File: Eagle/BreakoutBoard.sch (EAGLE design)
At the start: 13 parts

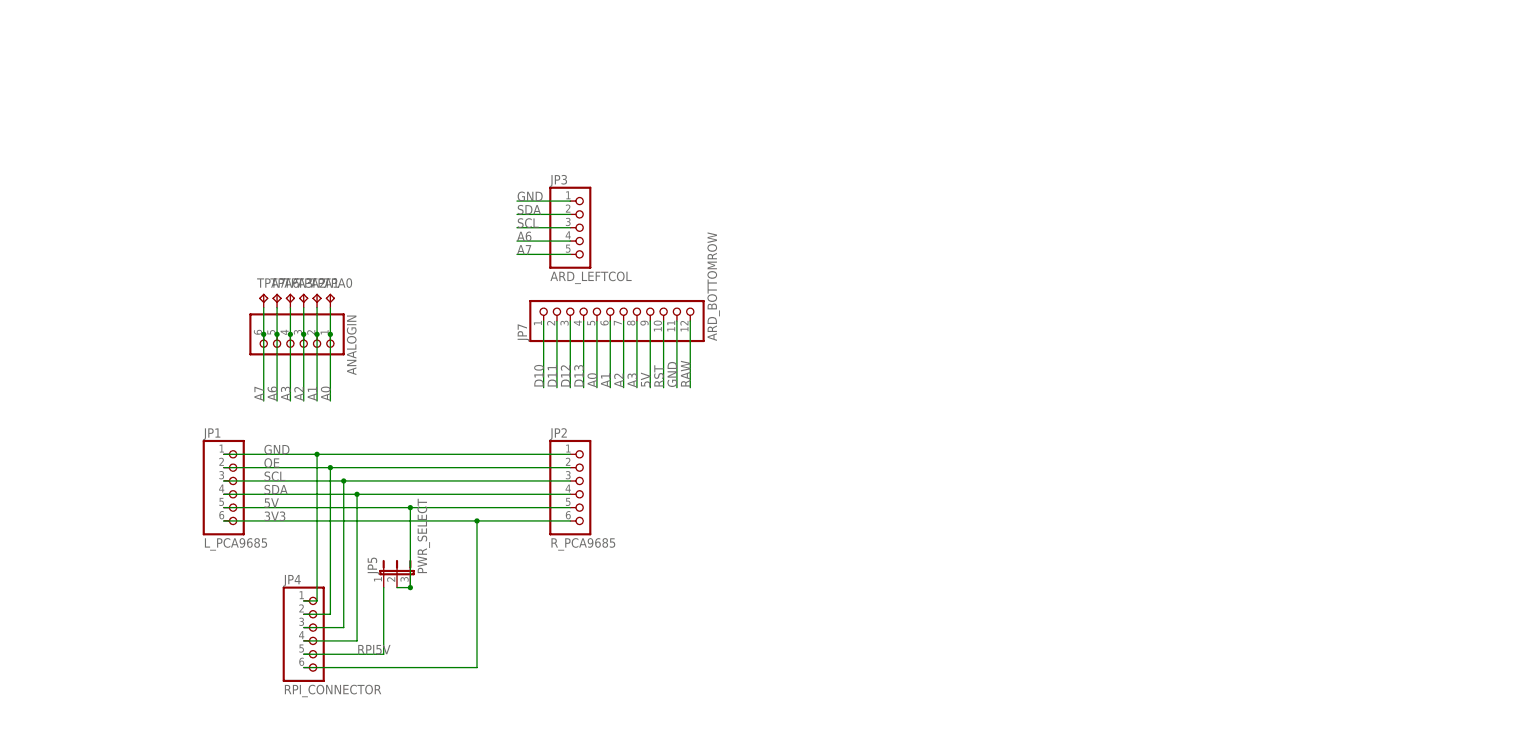
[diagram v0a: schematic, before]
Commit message: Routed board
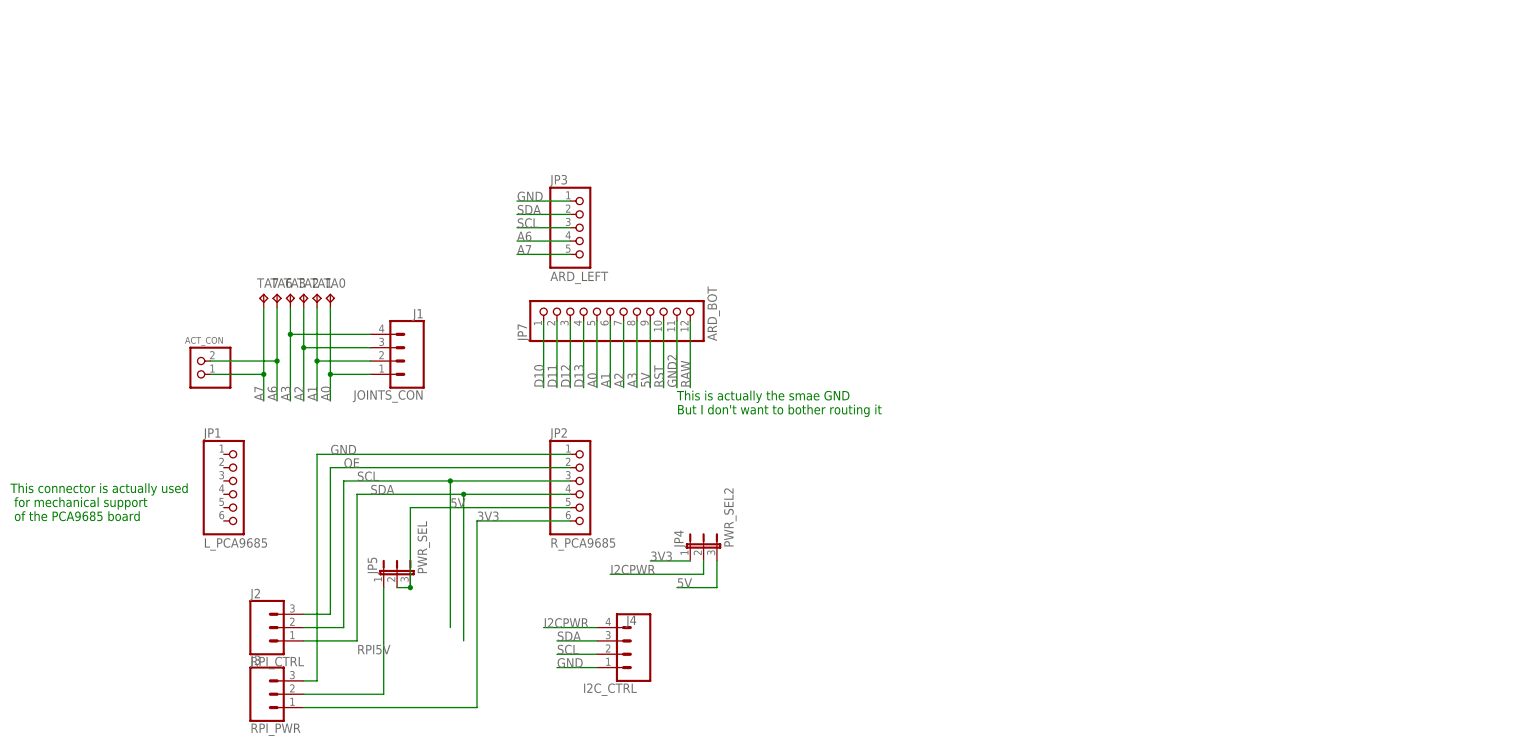
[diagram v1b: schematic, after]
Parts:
- removed ANALOGIN: (no value), pinhead:PINHD-1X6
- added ACT_CON: (no value), adafruit:JST_2PIN-THM
- added J1: JOINTS_CON, SparkFun-Connectors:CONN_04JST-PTH-VERT
- added J2: RPI_CTRL, SparkFun-Connectors:CONN_03JST-PTH-VERT
- added J3: RPI_PWR, SparkFun-Connectors:CONN_03JST-PTH-VERT
- added J4: I2C_CTRL, SparkFun-Connectors:CONN_04JST-PTH-VERT
- JP3: value ARD_LEFTCOL -> ARD_LEFT
- JP4: value RPI_CONNECTOR -> PWR_SEL2; device pinhead:PINHD-1X6 -> jumper:JP2E
- JP5: value PWR_SELECT -> PWR_SEL
- JP7: value ARD_BOTTOMROW -> ARD_BOT
- renumbered TPA0 to TA0, TPA1 to TA1, TPA2 to TA2, TPA3 to TA3, TPA6 to TA6, TPA7 to TA7
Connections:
- new net GND2: JP7.11
- new net I2CPWR: J4.4
- new net N$4: JP4.2
- net 3V3: now also J3.1, JP4.1; no longer JP1.6, JP4.6
- net 5V: now also JP4.3; no longer JP1.5
- net A0: now also J1.1; no longer ANALOGIN.1
- net A1: now also J1.2; no longer ANALOGIN.2
- net A2: now also J1.3; no longer ANALOGIN.3
- net A3: now also J1.4; no longer ANALOGIN.4
- net A6: now also ACT_CON.1; no longer ANALOGIN.5
- net A7: now also ACT_CON.2; no longer ANALOGIN.6
- net GND: now also J3.3, J4.1; no longer JP1.1, JP4.1, JP7.11
- net OE: now also J2.3; no longer JP1.2, JP4.2
- net RPI5V: now also J3.2; no longer JP4.5
- net SCL: now also J2.2, J4.2; no longer JP1.3, JP4.3
- net SDA: now also J2.1, J4.3; no longer JP1.4, JP4.4
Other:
- note added: "This connector is actually used for mechanical support of the PCA9685 board"
- note added: "This is actually the smae GND But I don't want to bother routing it"

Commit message: Added breakout board Added servo bracket renderings and dimensions
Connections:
- removed net GND2: JP7.11
- removed net N$4: JP4.2
- net 3V3: now also JP1.5, JP2.5; no longer JP2.6
- net 5V: now also JP1.6, JP2.6; no longer JP2.5
- net GND: now also JP1.1, JP7.11
- net I2CPWR: now also JP4.2
- net OE: now also JP1.2
- net SCL: now also JP1.3
- net SDA: now also JP1.4
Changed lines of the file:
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@@
 <pinref part="J3" gate="J$1" pin="3"/>
 <wire x1="66.04" y1="2.54" x2="63.5" y2="2.54" width="0.1524" layer="91"/>
+<pinref part="JP1" gate="A" pin="1"/>
+<wire x1="48.26" y1="45.72" x2="66.04" y2="45.72" width="0.1524" layer="91"/>
+<junction x="66.04" y="45.72"/>
+<label x="63.5" y="2.54" size="1.778" layer="95"/>
 </segment>
 <segment>
@@
 <wire x1="119.38" y1="5.08" x2="111.76" y2="5.08" width="0.1524" layer="91"/>
 <label x="111.76" y="5.08" size="1.778" layer="95"/>
+</segment>
+<segment>
+<pinref part="JP7" gate="G$1" pin="11"/>
+<wire x1="134.62" y1="71.12" x2="134.62" y2="58.42" width="0.1524" layer="91"/>
+<label x="134.62" y="58.42" size="1.778" layer="95" rot="R90"/>
 </segment>
 </net>
@@
 <wire x1="68.58" y1="15.24" x2="68.58" y2="43.18" width="0.1524" layer="91"/>
 <pinref part="J2" gate="J$1" pin="3"/>
+<pinref part="JP1" gate="A" pin="2"/>
+<wire x1="48.26" y1="43.18" x2="68.58" y2="43.18" width="0.1524" layer="91"/>
+<junction x="68.58" y="43.18"/>
 </segment>
 </net>
@@
 <pinref part="JP2" gate="A" pin="3"/>
 <label x="73.66" y="40.64" size="1.778" layer="95"/>
-<wire x1="71.12" y1="40.64" x2="91.44" y2="40.64" width="0.1524" layer="91"/>
-<wire x1="91.44" y1="40.64" x2="114.3" y2="40.64" width="0.1524" layer="91"/>
+<wire x1="71.12" y1="40.64" x2="114.3" y2="40.64" width="0.1524" layer="91"/>
 <wire x1="63.5" y1="12.7" x2="71.12" y2="12.7" width="0.1524" layer="91"/>
 <wire x1="71.12" y1="12.7" x2="71.12" y2="40.64" width="0.1524" layer="91"/>
 <pinref part="J2" gate="J$1" pin="2"/>
-<wire x1="91.44" y1="40.64" x2="91.44" y2="12.7" width="0.1524" layer="91"/>
-<junction x="91.44" y="40.64"/>
+<pinref part="JP1" gate="A" pin="3"/>
+<wire x1="48.26" y1="40.64" x2="71.12" y2="40.64" width="0.1524" layer="91"/>
+<junction x="71.12" y="40.64"/>
 </segment>
 <segment>
@@
 <pinref part="JP2" gate="A" pin="4"/>
 <label x="76.2" y="38.1" size="1.778" layer="95"/>
-<wire x1="73.66" y1="38.1" x2="93.98" y2="38.1" width="0.1524" layer="91"/>
-<wire x1="93.98" y1="38.1" x2="114.3" y2="38.1" width="0.1524" layer="91"/>
+<wire x1="73.66" y1="38.1" x2="114.3" y2="38.1" width="0.1524" layer="91"/>
 <wire x1="63.5" y1="10.16" x2="73.66" y2="10.16" width="0.1524" layer="91"/>
 <wire x1="73.66" y1="10.16" x2="73.66" y2="38.1" width="0.1524" layer="91"/>
 <pinref part="J2" gate="J$1" pin="1"/>
-<wire x1="93.98" y1="38.1" x2="93.98" y2="10.16" width="0.1524" layer="91"/>
-<junction x="93.98" y="38.1"/>
+<pinref part="JP1" gate="A" pin="4"/>
+<wire x1="48.26" y1="38.1" x2="73.66" y2="38.1" width="0.1524" layer="91"/>
+<junction x="73.66" y="38.1"/>
 </segment>
 <segment>
@@
 <net name="5V" class="0">
 <segment>
-<pinref part="JP2" gate="A" pin="5"/>
-<label x="91.44" y="35.56" size="1.778" layer="95"/>
+<label x="81.28" y="30.48" size="1.778" layer="95"/>
 <pinref part="JP5" gate="1" pin="3"/>
-<wire x1="83.82" y1="35.56" x2="114.3" y2="35.56" width="0.1524" layer="91"/>
 <wire x1="83.82" y1="20.32" x2="83.82" y2="35.56" width="0.1524" layer="91"/>
 <pinref part="JP5" gate="1" pin="2"/>
@@
 <label x="134.62" y="20.32" size="1.778" layer="95"/>
 </segment>
+<segment>
+<pinref part="JP1" gate="A" pin="6"/>
+<wire x1="48.26" y1="33.02" x2="48.26" y2="27.94" width="0.1524" layer="91"/>
+<wire x1="48.26" y1="33.02" x2="40.64" y2="33.02" width="0.1524" layer="91"/>
+<junction x="48.26" y="33.02"/>
+<label x="40.64" y="33.02" size="1.778" layer="95"/>
+</segment>
+<segment>
+<pinref part="JP2" gate="A" pin="6"/>
+<wire x1="114.3" y1="33.02" x2="104.14" y2="33.02" width="0.1524" layer="91"/>
+<label x="104.14" y="33.02" size="1.778" layer="95"/>
+</segment>
 </net>
 <net name="3V3" class="0">
 <segment>
-<pinref part="JP2" gate="A" pin="6"/>
-<label x="96.52" y="33.02" size="1.778" layer="95"/>
-<wire x1="96.52" y1="33.02" x2="114.3" y2="33.02" width="0.1524" layer="91"/>
-<wire x1="96.52" y1="-2.54" x2="96.52" y2="33.02" width="0.1524" layer="91"/>
 <pinref part="J3" gate="J$1" pin="1"/>
 <wire x1="96.52" y1="-2.54" x2="63.5" y2="-2.54" width="0.1524" layer="91"/>
+<label x="86.36" y="-2.54" size="1.778" layer="95"/>
 </segment>
 <segment>
@@
 <wire x1="137.16" y1="25.4" x2="129.54" y2="25.4" width="0.1524" layer="91"/>
 <label x="129.54" y="25.4" size="1.778" layer="95"/>
+</segment>
+<segment>
+<pinref part="JP2" gate="A" pin="5"/>
+<wire x1="114.3" y1="35.56" x2="104.14" y2="35.56" width="0.1524" layer="91"/>
+<label x="104.14" y="35.56" size="1.778" layer="95"/>
+</segment>
+<segment>
+<pinref part="JP1" gate="A" pin="5"/>
+<wire x1="48.26" y1="35.56" x2="40.64" y2="35.56" width="0.1524" layer="91"/>
+<label x="40.64" y="35.56" size="1.778" layer="95"/>
 </segment>
 </net>
@@
 <pinref part="J3" gate="J$1" pin="2"/>
 <wire x1="78.74" y1="0" x2="63.5" y2="0" width="0.1524" layer="91"/>
+<label x="71.12" y="0" size="1.778" layer="95"/>
 </segment>
 </net>
@@
 </segment>
 </net>
-<net name="GND2" class="0">
-<segment>
-<pinref part="JP7" gate="G$1" pin="11"/>
-<wire x1="134.62" y1="71.12" x2="134.62" y2="58.42" width="0.1524" layer="91"/>
-<label x="134.62" y="58.42" size="1.778" layer="95" rot="R90"/>
-</segment>
-</net>
 <net name="I2CPWR" class="0">
 <segment>
 <pinref part="J4" gate="G$1" pin="4"/>
-<wire x1="119.38" y1="12.7" x2="109.22" y2="12.7" width="0.1524" layer="91"/>
+<wire x1="119.38" y1="12.7" x2="106.68" y2="12.7" width="0.1524" layer="91"/>
 <label x="121.92" y="22.86" size="1.778" layer="95"/>
 <label x="109.22" y="12.7" size="1.778" layer="95"/>
 </segment>
-</net>
-<net name="N$4" class="0">
 <segment>
 <pinref part="JP4" gate="1" pin="2"/>
-<wire x1="139.7" y1="25.4" x2="139.7" y2="22.86" width="0.1524" layer="91"/>
-<wire x1="139.7" y1="22.86" x2="121.92" y2="22.86" width="0.1524" layer="91"/>
-</segment>
-</net>
+<wire x1="139.7" y1="25.4" x2="137.16" y2="22.86" width="0.1524" layer="91"/>
+<wire x1="137.16" y1="22.86" x2="119.38" y2="22.86" width="0.1524" layer="91"/>
+<label x="121.92" y="22.86" size="1.778" layer="95"/>
+</segment>
+</net>

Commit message: Done some refactoring and readjusting
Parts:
- removed ACT_CON: (no value), adafruit:JST_2PIN-THM
- removed J1: JOINTS_CON, SparkFun-Connectors:CONN_04JST-PTH-VERT
- removed J2: RPI_CTRL, SparkFun-Connectors:CONN_03JST-PTH-VERT
- removed J3: RPI_PWR, SparkFun-Connectors:CONN_03JST-PTH-VERT
- removed J4: I2C_CTRL, SparkFun-Connectors:CONN_04JST-PTH-VERT
- removed TA0, TA1, TA2, TA3, TA6, TA7: TPB1,27, testpad:TPB1,27
- added J5: RPIDATA, Connector:B3B-XH-A
- added J6: RPIPWR, Connector:B3B-XH-A
- added J7: I2C, Connector:B4B-XH-A
- added J8: JOINTS1234, Connector:B4B-XH-A
- added J9: JOINTS56, Connector:B2B-XH-A
- added JP10: SDA, Connector:PINHD-1X1
- added JP11, JP21, JP30, JP34: GND, Connector:PINHD-1X1
- added JP12: D10, Connector:PINHD-1X1
- added JP13: D11, Connector:PINHD-1X1
- added JP14: D12, Connector:PINHD-1X1
- added JP15: D13, Connector:PINHD-1X1
- added JP16: A0, Connector:PINHD-1X1
- added JP17: A1, Connector:PINHD-1X1
- added JP18: A2, Connector:PINHD-1X1
- added JP19: A3, Connector:PINHD-1X1
- added JP20: 5V, Connector:PINHD-1X1
- added JP22: RAW, Connector:PINHD-1X1
- added JP23: D8, Connector:PINHD-1X1
- added JP24: D7, Connector:PINHD-1X1
- added JP25: D6, Connector:PINHD-1X1
- added JP26: D5, Connector:PINHD-1X1
- added JP27: D4, Connector:PINHD-1X1
- added JP28: D3, Connector:PINHD-1X1
- added JP29: D2, Connector:PINHD-1X1
- added JP31: RST, Connector:PINHD-1X1
- added JP32: TRXI, Connector:PINHD-1X1
- added JP33, JP37: TX0, Connector:PINHD-1X1
- added JP35: A_VCC, Connector:PINHD-1X1
- added JP36: RXI, Connector:PINHD-1X1
- added JP38: DTR, Connector:PINHD-1X1
- added JP6: A7, Connector:PINHD-1X1
- added JP8: A6, Connector:PINHD-1X1
- added JP9: SCL, Connector:PINHD-1X1
- JP3: value ARD_LEFT -> D9; device pinhead:PINHD-1X5 -> Connector:PINHD-1X1
- JP7: value ARD_BOT -> RST; device pinhead:PINHD-1X12 -> Connector:PINHD-1X1
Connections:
- new net DTR: JP38.1
- new net RXI: JP36.1
- new net TX0: JP37.1
- net 3V3: now also J6.3; no longer J3.1
- net 5V: now also JP20.1, JP35.1; no longer JP7.9
- net A0: now also J8.1, JP16.1; no longer J1.1, JP7.5, TA0.TP
- net A1: now also J8.2, JP17.1; no longer J1.2, JP7.6, TA1.TP
- net A2: now also J8.3, JP18.1; no longer J1.3, JP7.7, TA2.TP
- net A3: now also J8.4, JP19.1; no longer J1.4, JP7.8, TA3.TP
- net A6: now also J9.2, JP8.1; no longer ACT_CON.1, JP3.4, TA6.TP
- net A7: now also J9.1, JP6.1; no longer ACT_CON.2, JP3.5, TA7.TP
- net D10: now also JP12.1; no longer JP7.1
- net D11: now also JP13.1; no longer JP7.2
- net D12: now also JP14.1; no longer JP7.3
- net D13: now also JP15.1; no longer JP7.4
- net GND: now also J6.1, J7.4, JP11.1, JP21.1, JP30.1, JP34.1; no longer J3.3, J4.1, JP3.1, JP7.11
- net I2CPWR: now also J7.1; no longer J4.4
- net OE: now also J5.1; no longer J2.3
- net RAW: now also JP22.1; no longer JP7.12
- net RPI5V: now also J6.2; no longer J3.2
- net RST: now also JP7.1; no longer JP7.10
- net SCL: now also J5.2, J7.3, JP9.1; no longer J2.2, J4.2, JP3.3
- net SDA: now also J5.3, J7.2, JP10.1; no longer J2.1, J4.3, JP3.2
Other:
- note removed: "This is actually the smae GND But I don't want to bother routing it"
